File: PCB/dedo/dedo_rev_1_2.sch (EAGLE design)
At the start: 11 parts

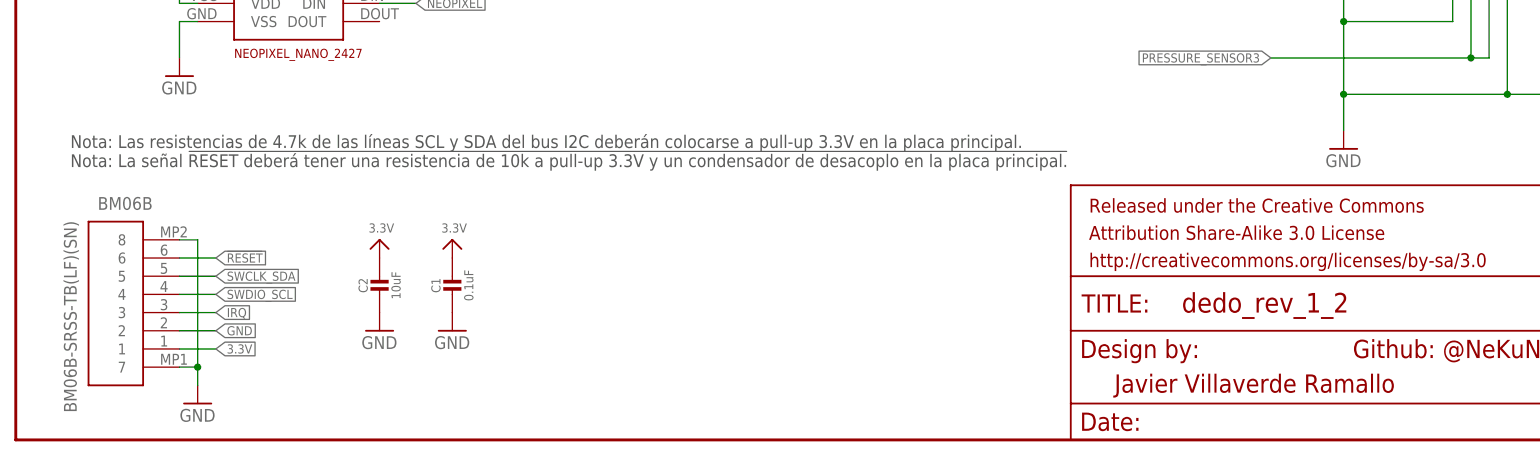
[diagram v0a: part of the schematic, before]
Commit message: Cambio de nombres y ubicación
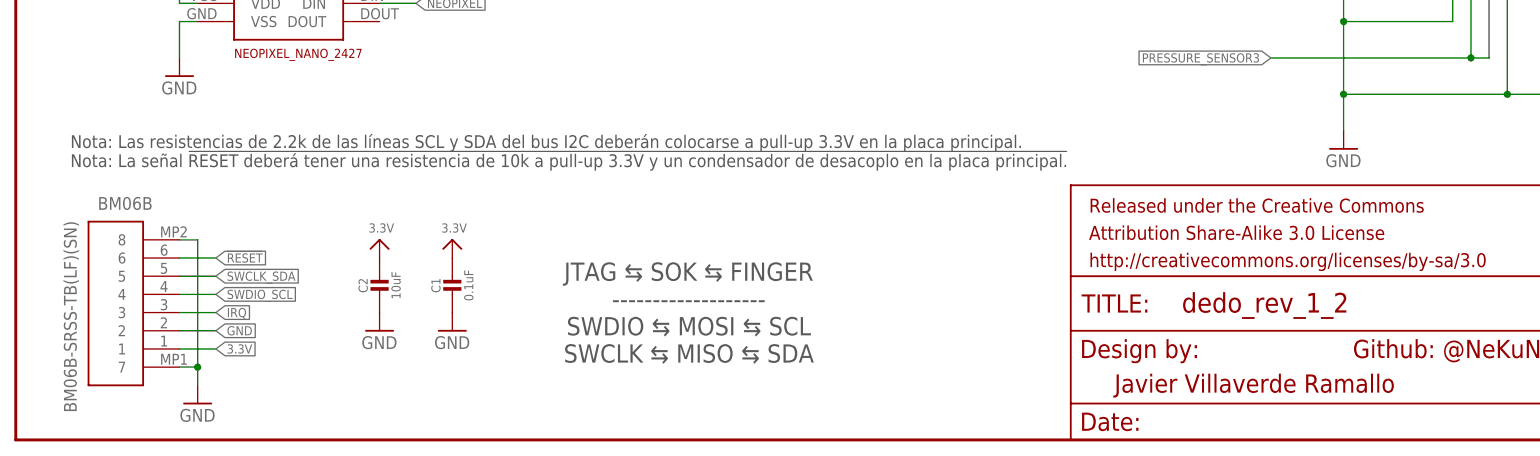
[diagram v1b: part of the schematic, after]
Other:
- note added: "JTAG ⇆ SOK ⇆ FINGER ------------------- SWDIO ⇆ MOSI ⇆ SCL SWCLK ⇆ MISO ⇆ SDA"
- note added: "Nota: Las resistencias de 2.2k de las líneas SCL y SDA del bus I2C deberán colocarse a pull-up 3.3V en la placa principal. Nota: La señal !RESET deberá tener una resistencia de 10k a pull-up 3.3V y un condensador de desacoplo en la placa principal."
- note removed: "Nota: Las resistencias de 4.7k de las líneas SCL y SDA del bus I2C deberán colocarse a pull-up 3.3V en la placa principal. Nota: La señal !RESET deberá tener una resistencia de 10k a pull-up 3.3V y un condensador de desacoplo en la placa principal."
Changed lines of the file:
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@@
 <sheet>
 <plain>
-<text x="7.62" y="38.1" size="1.778" layer="97">Nota: Las resistencias de 4.7k de las líneas SCL y SDA del bus I2C deberán colocarse a pull-up 3.3V en la placa principal.
+<text x="7.62" y="38.1" size="1.778" layer="97">Nota: Las resistencias de 2.2k de las líneas SCL y SDA del bus I2C deberán colocarse a pull-up 3.3V en la placa principal.
 Nota: La señal !RESET deberá tener una resistencia de 10k a pull-up 3.3V y un condensador de desacoplo en la placa principal.</text>
 <text x="186.69" y="11.43" size="2.54" layer="94">Github: @NeKuNeKo</text>
@@
 0x40 - 0x20
 0x4f - 0x2f</text>
+<text x="93.98" y="17.78" size="2.54" layer="97" ratio="15" align="center">JTAG ⇆ SOK ⇆ FINGER
+-------------------
+SWDIO ⇆ MOSI ⇆ SCL
+SWCLK ⇆ MISO ⇆ SDA</text>
 </plain>
 <instances>
